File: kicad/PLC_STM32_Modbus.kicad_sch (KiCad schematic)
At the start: 0 parts

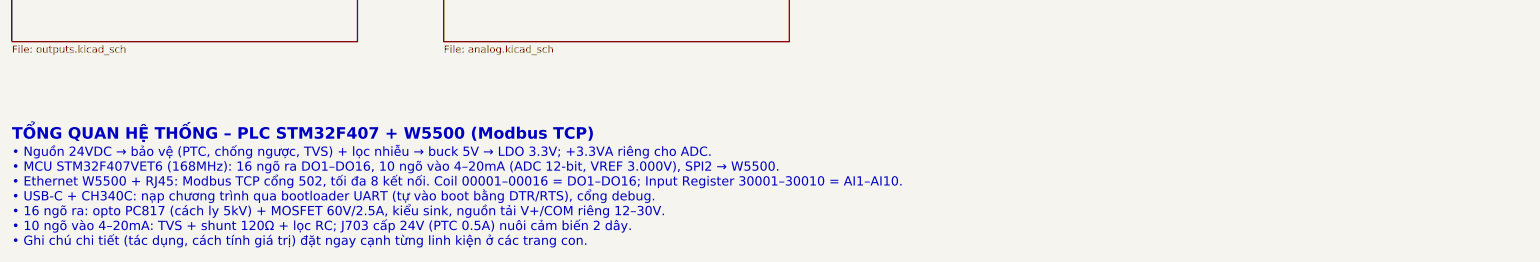
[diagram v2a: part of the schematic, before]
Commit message: - thay w5500 bằng module w5500 lite
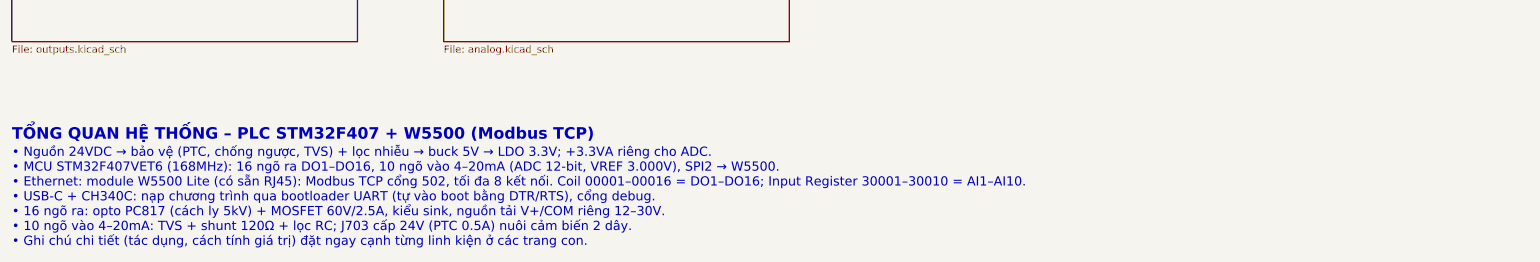
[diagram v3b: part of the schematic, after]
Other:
- note added: "• Nguồn 24VDC → bảo vệ (PTC, chống ngược, TVS) + lọc nhiễu → buck 5V → LDO 3.3V; +3.3VA riêng cho ADC. • MCU STM32F407VET6 (168MHz): 16 ngõ ra DO1–DO16, 10 ngõ vào 4–20mA (ADC 12-bit, VREF 3.000V), SPI2 → W5500. • Ethernet: module W5500 Lite (có sẵn RJ45): Modbus TCP cổng 502, tối đa 8 kết nối. Coil 00001–00016 = DO1–DO16; Input Register 30001–30010 = AI1–AI10. • USB-C + CH340C: nạp chương trình 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"
- note removed: "• Nguồn 24VDC → bảo vệ (PTC, chống ngược, TVS) + lọc nhiễu → buck 5V → LDO 3.3V; +3.3VA riêng cho ADC. • MCU STM32F407VET6 (168MHz): 16 ngõ ra DO1–DO16, 10 ngõ vào 4–20mA (ADC 12-bit, VREF 3.000V), SPI2 → W5500. • Ethernet W5500 + RJ45: Modbus TCP cổng 502, tối đa 8 kết nối. Coil 00001–00016 = DO1–DO16; Input Register 30001–30010 = AI1–AI10. • USB-C + CH340C: nạp chương trình qua bootloader UART 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"
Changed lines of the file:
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@@
 		)
 	)
-	(text "• Nguồn 24VDC → bảo vệ (PTC, chống ngược, TVS) + lọc nhiễu → buck 5V → LDO 3.3V; +3.3VA riêng cho ADC.\n• MCU STM32F407VET6 (168MHz): 16 ngõ ra DO1–DO16, 10 ngõ vào 4–20mA (ADC 12-bit, VREF 3.000V), SPI2 → W5500.\n• Ethernet W5500 + RJ45: Modbus TCP cổng 502, tối đa 8 kết nối. Coil 00001–00016 = DO1–DO16; Input Register 30001–30010 = AI1–AI10.\n• USB-C + CH340C: nạp chương trình qua bootloader UART (tự vào boot bằng DTR/RTS), cổng debug.\n• 16 ngõ ra: opto PC817 (cách ly 5kV) + MOSFET 60V/2.5A, kiểu sink, nguồn tải V+/COM riêng 12–30V.\n• 10 ngõ vào 4–20mA: TVS + shunt 120Ω + lọc RC; J703 cấp 24V (PTC 0.5A) nuôi cảm biến 2 dây.\n• Ghi chú chi tiết (tác dụng, cách tính giá trị) đặt ngay cạnh từng linh kiện ở các trang con."
+	(text "• Nguồn 24VDC → bảo vệ (PTC, chống ngược, TVS) + lọc nhiễu → buck 5V → LDO 3.3V; +3.3VA riêng cho ADC.\n• MCU STM32F407VET6 (168MHz): 16 ngõ ra DO1–DO16, 10 ngõ vào 4–20mA (ADC 12-bit, VREF 3.000V), SPI2 → W5500.\n• Ethernet: module W5500 Lite (có sẵn RJ45): Modbus TCP cổng 502, tối đa 8 kết nối. Coil 00001–00016 = DO1–DO16; Input Register 30001–30010 = AI1–AI10.\n• USB-C + CH340C: nạp chương trình qua bootloader UART (tự vào boot bằng DTR/RTS), cổng debug.\n• 16 ngõ ra: opto PC817 (cách ly 5kV) + MOSFET 60V/2.5A, kiểu sink, nguồn tải V+/COM riêng 12–30V.\n• 10 ngõ vào 4–20mA: TVS + shunt 120Ω + lọc RC; J703 cấp 24V (PTC 0.5A) nuôi cảm biến 2 dây.\n• Ghi chú chi tiết (tác dụng, cách tính giá trị) đặt ngay cạnh từng linh kiện ở các trang con."
 		(exclude_from_sim no)
 		(at 30 128.4 0)
@@
 	)
 	(sheet
+		(at 30 85)
+		(size 60 25)
+		(exclude_from_sim no)
+		(in_bom yes)
+		(on_board yes)
+		(dnp no)
+		(stroke
+			(width 0.1524)
+			(type solid)
+		)
+		(fill
+			(color 0 0 0 0)
+		)
+		(property "Sheetname" "16 ngo ra transistor"
+			(at 30 84.2 0)
+			(show_name no)
+			(do_not_autoplace no)
+			(effects
+				(font
+					(size 1.524 1.524)
+				)
+				(justify left bottom)
+			)
+		)
+		(property "Sheetfile" "outputs.kicad_sch"
+			(at 30 110.6 0)
+			(show_name no)
+			(do_not_autoplace no)
+			(effects
+				(font
+					(size 1.27 1.27)
+				)
+				(justify left top)
+			)
+		)
+		(instances
+			(project "PLC_STM32_Modbus"
+				(path "/2be3e191-9af5-421c-aa34-3e3c37fa6c43"
+					(page "3")
+				)
+			)
+		)
+	)
+	(sheet
+		(at 105 85)
+		(size 60 25)
+		(exclude_from_sim no)
+		(in_bom yes)
+		(on_board yes)
+		(dnp no)
+		(stroke
+			(width 0.1524)
+			(type solid)
+		)
+		(fill
+			(color 0 0 0 0)
+		)
+		(property "Sheetname" "10 ngo vao analog"
+			(at 105 84.2 0)
+			(show_name no)
+			(do_not_autoplace no)
+			(effects
+				(font
+					(size 1.524 1.524)
+				)
+				(justify left bottom)
+			)
+		)
+		(property "Sheetfile" "analog.kicad_sch"
+			(at 105 110.6 0)
+			(show_name no)
+			(do_not_autoplace no)
+			(effects
+				(font
+					(size 1.27 1.27)
+				)
+				(justify left top)
+			)
+		)
+		(instances
+			(project "PLC_STM32_Modbus"
+				(path "/2be3e191-9af5-421c-aa34-3e3c37fa6c43"
+					(page "5")
+				)
+			)
+		)
+	)
+	(sheet
+		(at 180 40)
+		(size 60 25)
+		(exclude_from_sim no)
+		(in_bom yes)
+		(on_board yes)
+		(dnp no)
+		(stroke
+			(width 0.1524)
+			(type solid)
+		)
+		(fill
+			(color 0 0 0 0)
+		)
+		(property "Sheetname" "USB nap code"
+			(at 180 39.2 0)
+			(show_name no)
+			(do_not_autoplace no)
+			(effects
+				(font
+					(size 1.524 1.524)
+				)
+				(justify left bottom)
+			)
+		)
+		(property "Sheetfile" "usb.kicad_sch"
+			(at 180 65.6 0)
+			(show_name no)
+			(do_not_autoplace no)
+			(effects
+				(font
+					(size 1.27 1.27)
+				)
+				(justify left top)
+			)
+		)
+		(instances
+			(project "PLC_STM32_Modbus"
+				(path "/2be3e191-9af5-421c-aa34-3e3c37fa6c43"
+					(page "6")
+				)
+			)
+		)
+	)
+	(sheet
 		(at 30 40)
 		(size 60 25)
@@
 				)
 			)
-		)
-	)
-	(sheet
-		(at 30 85)
-		(size 60 25)
-		(exclude_from_sim no)
-		(in_bom yes)
-		(on_board yes)
-		(dnp no)
-		(stroke
-			(width 0.1524)
-			(type solid)
-		)
-		(fill
-			(color 0 0 0 0)
-		)
-		(property "Sheetname" "16 ngo ra transistor"
-			(at 30 84.2 0)
-			(show_name no)
-			(do_not_autoplace no)
-			(effects
-				(font
-					(size 1.524 1.524)
-				)
-				(justify left bottom)
-			)
-		)
-		(property "Sheetfile" "outputs.kicad_sch"
-			(at 30 110.6 0)
-			(show_name no)
-			(do_not_autoplace no)
-			(effects
-				(font
-					(size 1.27 1.27)
-				)
-				(justify left top)
-			)
-		)
-		(instances
-			(project "PLC_STM32_Modbus"
-				(path "/2be3e191-9af5-421c-aa34-3e3c37fa6c43"
-					(page "3")
-				)
-			)
-		)
-	)
-	(sheet
-		(at 180 40)
-		(size 60 25)
-		(exclude_from_sim no)
-		(in_bom yes)
-		(on_board yes)
-		(dnp no)
-		(stroke
-			(width 0.1524)
-			(type solid)
-		)
-		(fill
-			(color 0 0 0 0)
-		)
-		(property "Sheetname" "USB nap code"
-			(at 180 39.2 0)
-			(show_name no)
-			(do_not_autoplace no)
-			(effects
-				(font
-					(size 1.524 1.524)
-				)
-				(justify left bottom)
-			)
-		)
-		(property "Sheetfile" "usb.kicad_sch"
-			(at 180 65.6 0)
-			(show_name no)
-			(do_not_autoplace no)
-			(effects
-				(font
-					(size 1.27 1.27)
-				)
-				(justify left top)
-			)
-		)
-		(instances
-			(project "PLC_STM32_Modbus"
-				(path "/2be3e191-9af5-421c-aa34-3e3c37fa6c43"
-					(page "6")
-				)
-			)
-		)
-	)
-	(sheet
-		(at 105 85)
-		(size 60 25)
-		(exclude_from_sim no)
-		(in_bom yes)
-		(on_board yes)
-		(dnp no)
-		(stroke
-			(width 0.1524)
-			(type solid)
-		)
-		(fill
-			(color 0 0 0 0)
-		)
-		(property "Sheetname" "10 ngo vao analog"
-			(at 105 84.2 0)
-			(show_name no)
-			(do_not_autoplace no)
-			(effects
-				(font
-					(size 1.524 1.524)
-				)
-				(justify left bottom)
-			)
-		)
-		(property "Sheetfile" "analog.kicad_sch"
-			(at 105 110.6 0)
-			(show_name no)
-			(do_not_autoplace no)
-			(effects
-				(font
-					(size 1.27 1.27)
-				)
-				(justify left top)
-			)
-		)
-		(instances
-			(project "PLC_STM32_Modbus"
-				(path "/2be3e191-9af5-421c-aa34-3e3c37fa6c43"
-					(page "5")
-				)
-			)
